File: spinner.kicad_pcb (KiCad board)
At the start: 2 copper layers, 190 x 190 mm, 102 parts, among them J1 Micro_SD_Card, SW1 SW_SPDT, U1 AP63205WU, U2 RS0102, U3 SFH617A-3X006, U4 SFH617A-3X006, U5 SFH617A-3X006

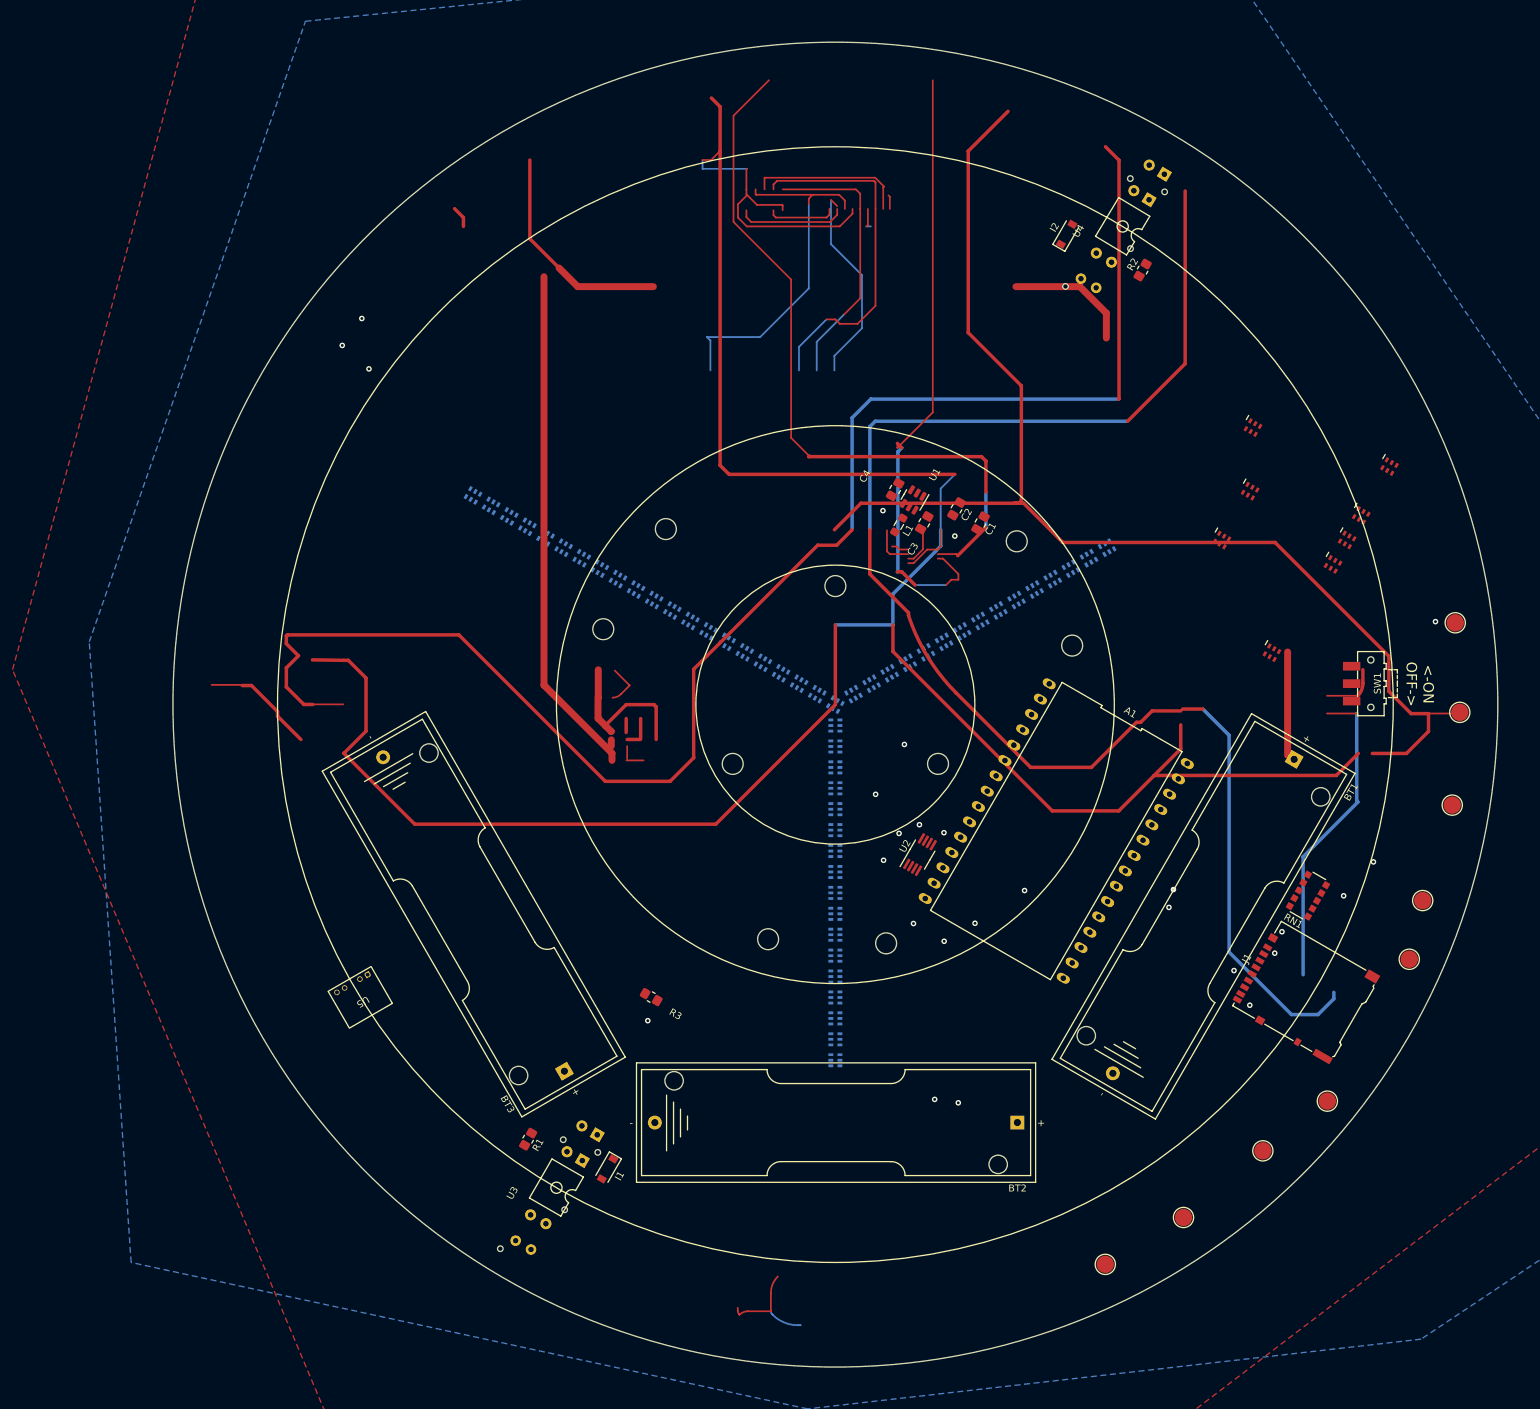
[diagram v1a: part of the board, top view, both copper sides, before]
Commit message: Push LEDs around and shrink board.
Leaning towards using 3 14500 3.7v batteries.
And figuring out on-board charging.
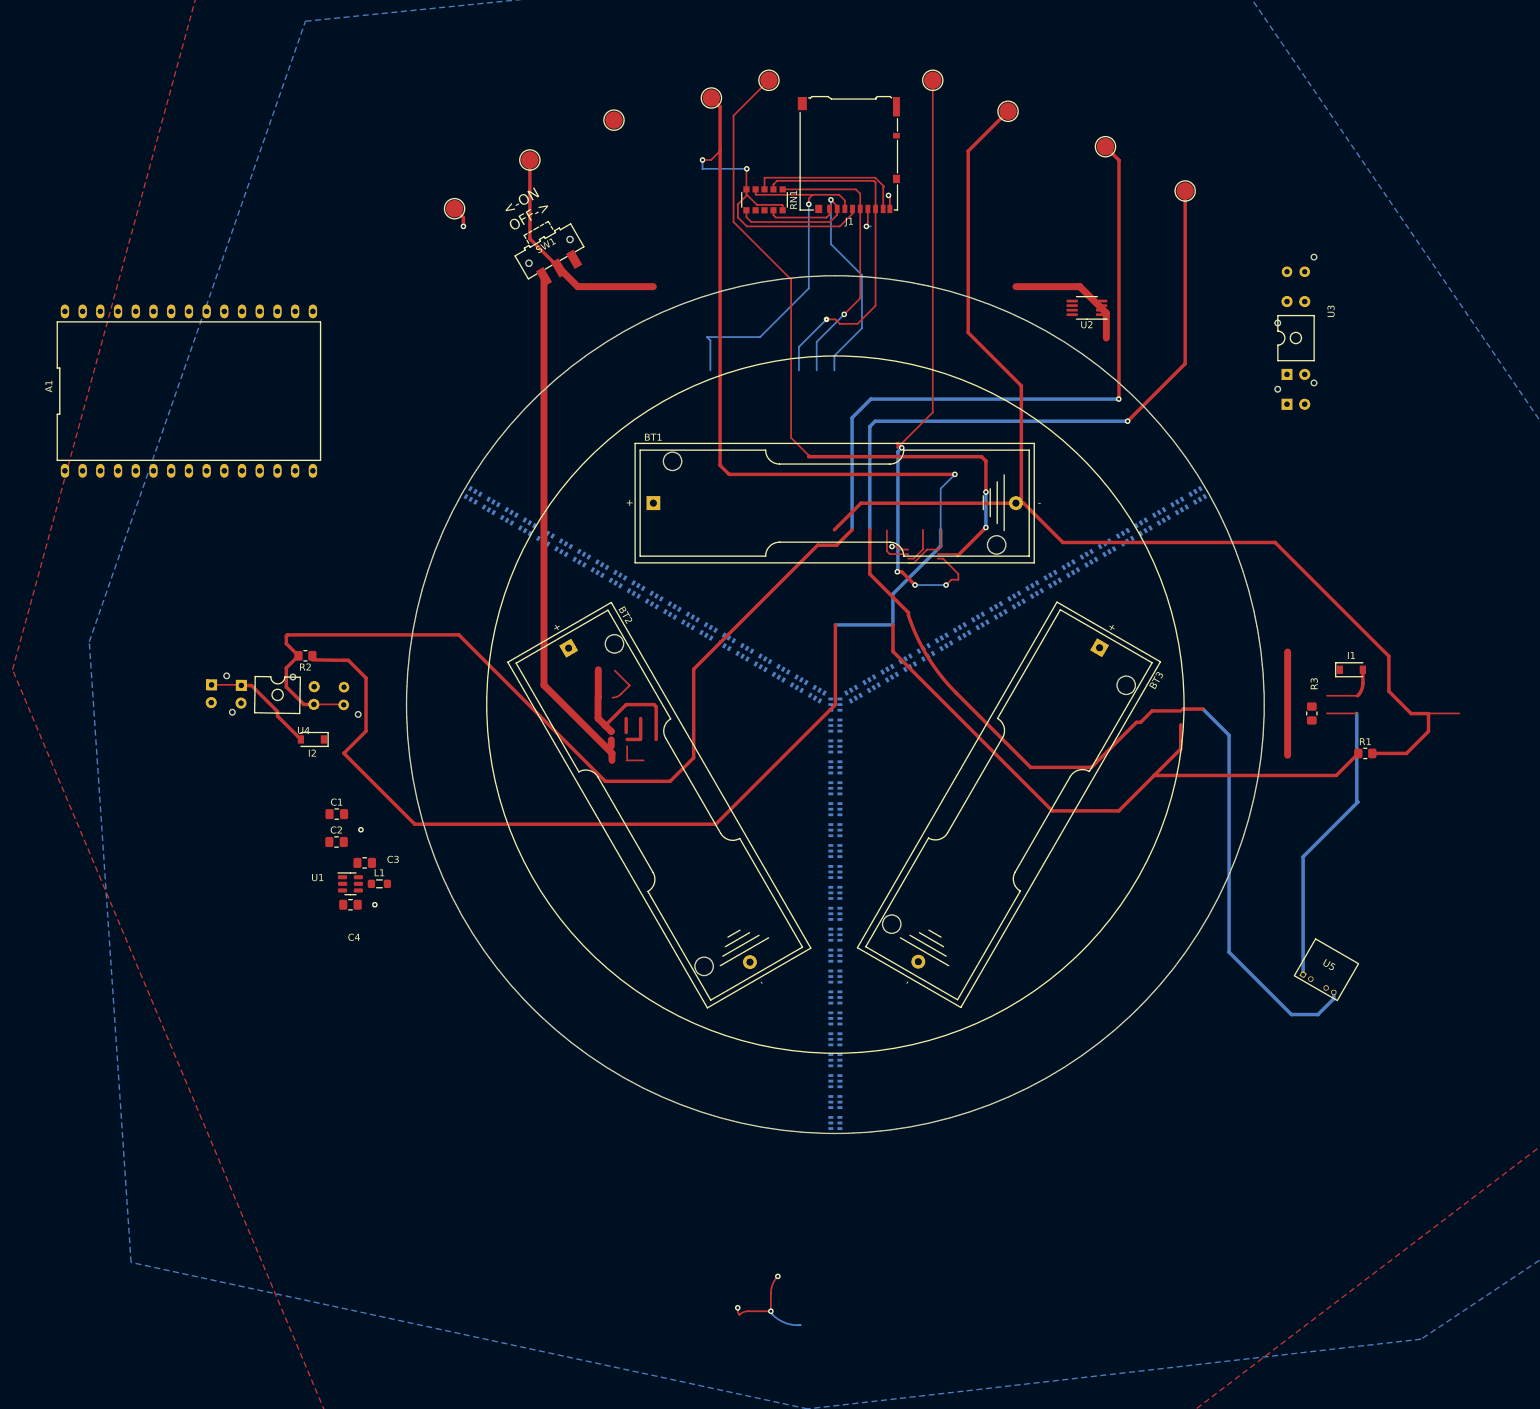
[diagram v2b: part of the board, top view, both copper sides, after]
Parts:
- removed H1, H2, H3, H4, H5, H6, H7, H8, H9: MountingHole, MountingHole:MountingHole_3mm
- D216, D217, D218, D219, D220, D318, D319, D320: moved to B.Cu
- moved U3 161.5 mm to (216.0, 47.4), turned to 90 degrees
- moved TP5 157.0 mm to (164.0, 10.5), turned to 0 degrees
- moved TP1 156.0 mm to (140.5, 10.5), turned to 0 degrees
- moved TP2 155.3 mm to (95.4, 28.9), turned to 0 degrees
- moved TP4 155.2 mm to (118.2, 16.2), turned to 0 degrees
- moved TP9 155.1 mm to (106.2, 21.9), turned to 0 degrees
- moved TP6 154.4 mm to (200.2, 26.3), turned to 0 degrees
- moved TP7 154.0 mm to (188.7, 20.0), turned to 0 degrees
- moved TP3 153.8 mm to (132.2, 13.0), turned to 0 degrees
- moved TP8 153.5 mm to (174.8, 14.9), turned to 0 degrees
- moved A1 139.5 mm to (57.3, 55.0), turned to 0 degrees
- moved U4 138.6 mm to (70.0, 98.6), turned to -1 degrees
- moved U5 138.6 mm to (219.3, 140.0), turned to -30 degrees
- moved J1 136.6 mm to (151.9, 21.2), turned to 180 degrees
- moved SW1 133.1 mm to (109.0, 35.0), turned to -150 degrees
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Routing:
- net /OPTO_in_2: track 179.7 -> 216.1 mm, vias 2 -> 1
- net Net-(D315-Pad6): track 36.4 -> 0.00 mm
- net Net-(BT1-Pad2): track 0.00 -> 18.1 mm
- net /OPTO_in_1: track 240.6 -> 222.5 mm
- net +BATT: track 46.7 -> 31.9 mm
- net Net-(BT2-Pad2): track 0.00 -> 14.8 mm
- net /CI: track 95.8 -> 104.5 mm
- net GND: track 45.8 -> 37.1 mm
- net unconnected-(SW1-Pad1): track 8.21 -> 0.00 mm
- net Net-(I1-Pad2): track 0.00 -> 8.21 mm
- net Net-(C3-Pad1): track 10.3 -> 4.79 mm
- net /GPIO_13: track 0.00 -> 5.47 mm
- net +3V3: vias 5 -> 3
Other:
- board size 190 x 190 mm -> 123 x 123 mm

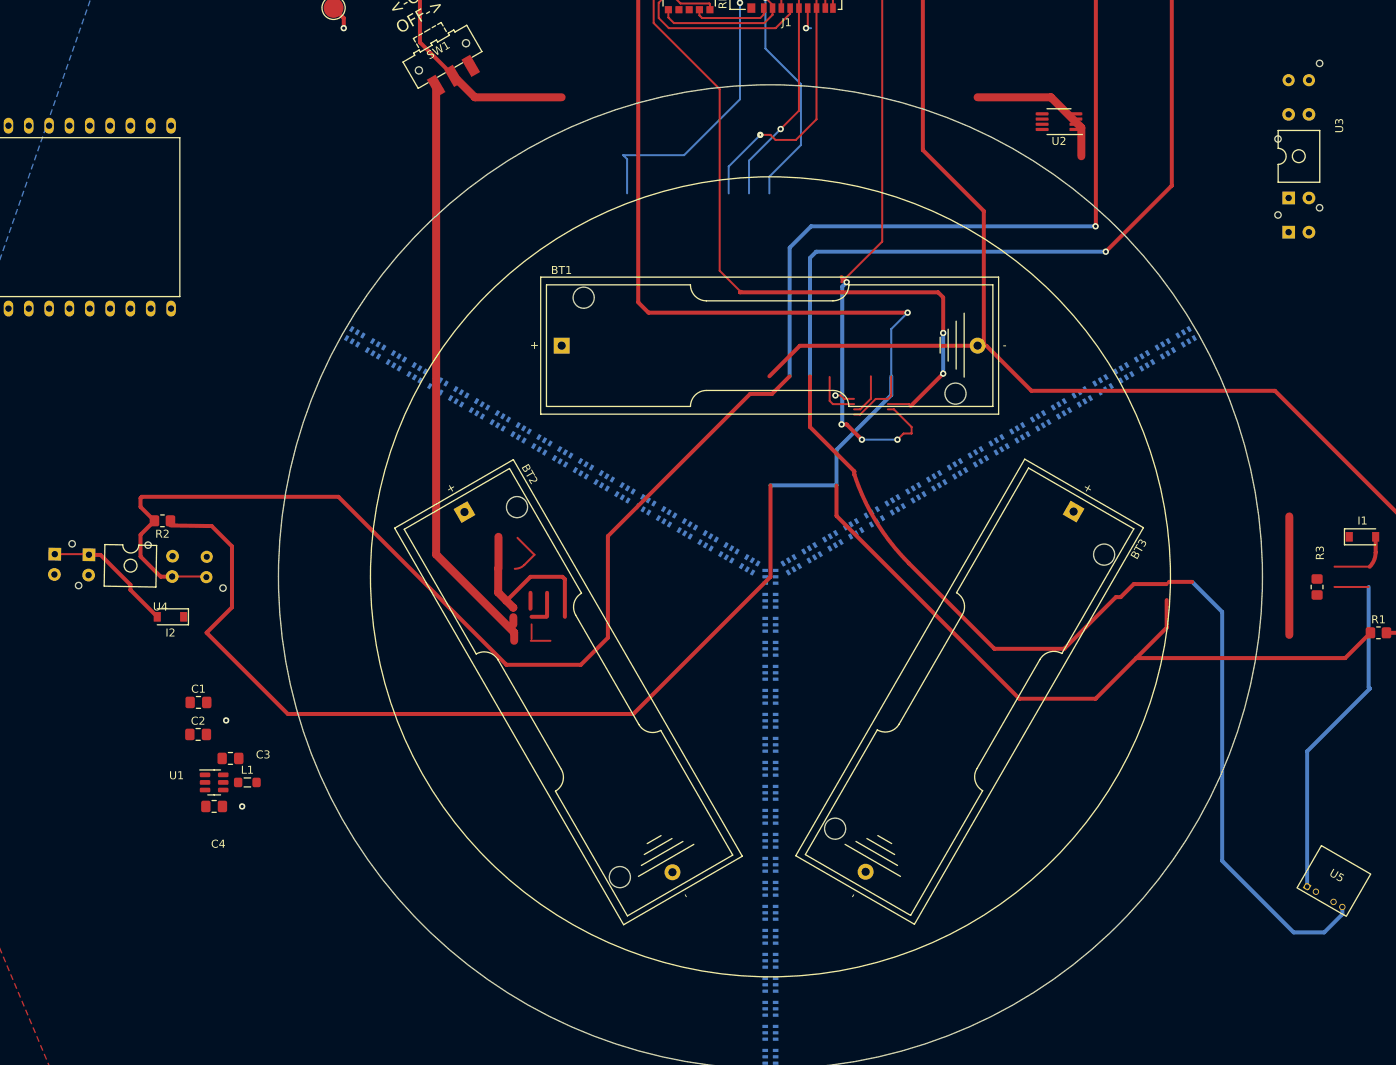
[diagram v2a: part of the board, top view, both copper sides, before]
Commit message: Found a couple parts for bom.
Chose some through beam things,
ESP32 module.
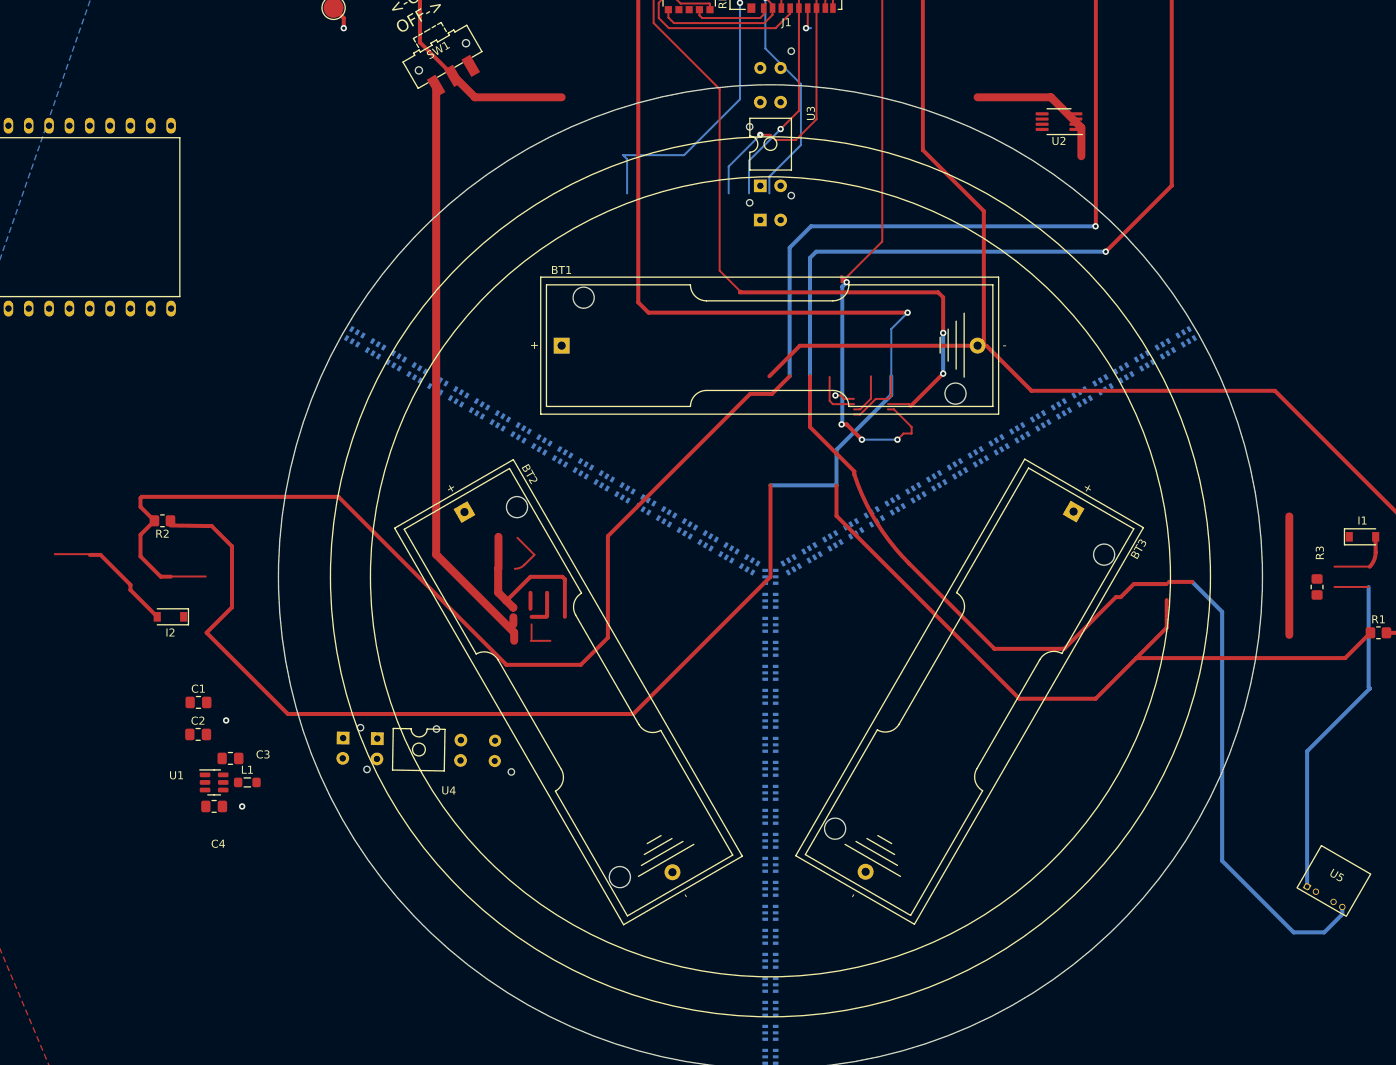
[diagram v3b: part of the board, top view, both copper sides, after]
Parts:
- moved U3 66.1 mm to (150.0, 45.9)
- moved U4 42.8 mm to (106.1, 121.6)
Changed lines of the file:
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@@
   )
   (footprint "Library:MULTI_PART_THRU_BEAM" (layer "F.Cu")
-    (at 216.04 47.422 90)
+    (at 150 45.898 90)
     (descr "4-lead though-hole mounted DIP package, row spacing 10.16 mm (400 mils)")
     (tags "THT DIP DIL PDIP 2.54mm 10.16mm 400mil")
@@
   )
   (footprint "Library:MULTI_PART_THRU_BEAM" (layer "F.Cu")
-    (at 70.012184 98.603807 -1)
+    (at 106.058 121.59 -1)
     (descr "4-lead though-hole mounted DIP package, row spacing 10.16 mm (400 mils)")
     (tags "THT DIP DIL PDIP 2.54mm 10.16mm 400mil")
@@
   )
   (gr_circle (center 150 100) (end 200 100) (layer "F.SilkS") (width 0.15) (fill none))
+  (gr_circle (center 150 100) (end 205 100) (layer "F.SilkS") (width 0.15) (fill none))
   (gr_circle (center 150 100) (end 211.5 100) (layer "Edge.Cuts") (width 0.1) (fill none))
   (gr_text "<-ON\nOFF->" (at 105.55 28.88 -330) (layer "F.SilkS")

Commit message: IDK.  Adding lib things.  Need to update kicad.
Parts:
- removed A1: Adafruit_HUZZAH_ESP8266_breakout, Library:huzz_hakz
- added D121: APA102, Library:SK9822-hakz, B.Cu at (150.0, 163.0)
- added D122: APA102, Library:SK9822-hakz, B.Cu at (150.0, 166.0)
- added D123: APA102, Library:SK9822-hakz, B.Cu at (150.0, 169.0)
- added D124: APA102, Library:SK9822-hakz, B.Cu at (150.0, 172.0)
- added D221: APA102, Library:SK9822-hakz, B.Cu at (95.4, 68.5)
- added D222: APA102, Library:SK9822-hakz, B.Cu at (92.8, 67.0)
- added D223: APA102, Library:SK9822-hakz, B.Cu at (90.2, 65.5)
- added D224: APA102, Library:SK9822-hakz, B.Cu at (87.6, 64.0)
- added D321: APA102, Library:SK9822-hakz, B.Cu at (204.6, 68.5)
- added D322: APA102, Library:SK9822-hakz, B.Cu at (207.2, 67.0)
- added D323: APA102, Library:SK9822-hakz, B.Cu at (209.8, 65.5)
- added D324: APA102, Library:SK9822-hakz, B.Cu at (212.4, 64.0)
- added H1: MountingHole, MountingHole:MountingHole_3mm, F.Cu at (50.4, 32.9)
- added H2: MountingHole, MountingHole:MountingHole_3mm, F.Cu at (50.4, 25.4)
- added H3: MountingHole, MountingHole:MountingHole_3mm, F.Cu at (58.0, 25.4)
- added H4: MountingHole, MountingHole:MountingHole_3mm, F.Cu at (42.9, 25.4)
- added H5: MountingHole, MountingHole:MountingHole_3mm, F.Cu at (65.5, 25.4)
- added H6: MountingHole, MountingHole:MountingHole_3mm, F.Cu at (50.4, 40.5)
- added H7: MountingHole, MountingHole:MountingHole_3mm, F.Cu at (42.9, 32.9)
- added H8: MountingHole, MountingHole:MountingHole_3mm, F.Cu at (58.0, 32.9)
- added H9: MountingHole, MountingHole:MountingHole_3mm, F.Cu at (42.9, 40.5)
- added U6: ESP32-WROVER, Library:ESP32-WROVER, F.Cu at (138.8, 82.5)
- moved J1 137.8 mm to (150.0, 159.0), turned to 0 degrees
- moved U3 129.6 mm to (278.3, 27.1)
- moved U4 86.2 mm to (27.1, 156.1)
- moved U2 79.9 mm to (262.5, 20.0)
- moved C4 60.0 mm to (20.6, 132.8)
- moved C1 60.0 mm to (18.6, 119.8)
- moved C3 60.0 mm to (22.6, 126.8)
- moved L1 60.0 mm to (24.7, 129.8)
- moved R2 60.0 mm to (14.1, 97.1)
- moved C2 60.0 mm to (18.6, 123.8)
- moved U1 60.0 mm to (20.6, 129.8)
- moved I2 60.0 mm to (15.1, 109.1)
- moved R1 53.5 mm to (278.3, 118.3)
- moved R3 53.5 mm to (270.6, 112.6)
- moved I1 53.5 mm to (276.3, 106.3)
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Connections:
- D120 pad 5: /CO_1 -> Net-(D120-Pad5)
- D120 pad 6: /DO_1 -> Net-(D120-Pad6)
- D220 pad 5: /CO_3 -> Net-(D220-Pad5)
- D220 pad 6: /DO_3 -> Net-(D220-Pad6)
- D320 pad 5: unconnected-(D320-Pad5) -> Net-(D320-Pad5)
- D320 pad 6: unconnected-(D320-Pad6) -> Net-(D320-Pad6)
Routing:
- net +3V3: track 378.4 -> 172.1 mm
- net unconnected-(U6-Pad9): track 0.00 -> 114.1 mm
- net unconnected-(U6-Pad16): track 0.00 -> 92.3 mm
- net unconnected-(U6-Pad24): track 0.00 -> 21.0 mm
- net Net-(BT1-Pad2): track 18.1 -> 0.00 mm
- net /DI: track 88.9 -> 107.1 mm
- net Net-(BT2-Pad2): track 14.8 -> 0.00 mm
- net unconnected-(SW1-Pad1): track 0.00 -> 8.21 mm
- net Net-(I1-Pad2): track 8.21 -> 0.00 mm
- net /GPIO_14: track 6.21 -> 0.00 mm
- net unconnected-(U6-Pad20): track 0.00 -> 5.47 mm
- net /GPIO_13: track 5.47 -> 0.00 mm
- net GND: vias 9 -> 6
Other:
- board size 123 x 123 mm -> 147 x 147 mm

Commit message: Placed battery and test points, cpu, reduced copmlexity by %50 for %80 of pins.
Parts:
- removed G***: LOGO, Library:hakz_04
- U6: value ESP32-WROVER -> ESP32-S3-WROOM-1; footprint Library:ESP32-WROVER -> Library:ESP32-S3-WROOM-1
- moved U3 96.5 mm to (215.0, 100.0), turned to 180 degrees
- moved U4 80.7 mm to (85.0, 100.0)
- moved TP2 54.6 mm to (150.0, 30.0)
- moved U6 30.6 mm to (150.0, 54.0), turned to 0 degrees
- moved TP1 29.9 mm to (162.2, 31.1)
- moved TP6 28.9 mm to (203.6, 55.0)
- moved TP7 27.1 mm to (195.0, 46.4)
- moved TP8 26.5 mm to (185.0, 39.4)
- moved TP5 25.8 mm to (173.9, 34.2)
- moved TP4 19.7 mm to (126.1, 34.2)
- moved TP9 19.6 mm to (115.0, 39.4)
- moved TP3 18.9 mm to (137.8, 31.1)
- moved RN1 14.3 mm to (150.9, 18.5)
- moved BT1 14.0 mm to (150.0, 74.0), turned to 180 degrees
- moved SW1 12.1 mm to (105.0, 46.4), turned to -140 degrees
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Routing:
- net /OPTO_in_1: track 222.5 -> 0.00 mm, vias 1 -> 0
- net /OPTO_in_2: track 216.1 -> 0.00 mm, vias 1 -> 0
- net /OPTO_in_0: track 180.9 -> 0.00 mm
- net +3V3: track 172.1 -> 0.00 mm, vias 3 -> 0
- net unconnected-(U6-Pad9): track 114.1 -> 0.00 mm
- net /DI: track 107.1 -> 0.00 mm, vias 4 -> 0
- net /CI: track 104.5 -> 0.00 mm, vias 2 -> 0
- net unconnected-(U6-Pad16): track 92.3 -> 0.00 mm
- net Net-(C4-Pad1): track 74.3 -> 0.00 mm
- net /spi_out: track 51.2 -> 0.00 mm, vias 1 -> 0
- net /spi_in: track 50.7 -> 0.00 mm, vias 1 -> 0
- net Net-(U3-Pad2): track 45.0 -> 0.00 mm
- net /spi_cs: track 44.8 -> 0.00 mm, vias 1 -> 0
- net /spi_clk: track 39.3 -> 0.00 mm, vias 1 -> 0
- net GND: track 37.1 -> 0.00 mm, vias 6 -> 0
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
